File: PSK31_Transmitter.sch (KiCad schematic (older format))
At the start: 5 parts

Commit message: Add microcontroller and pll
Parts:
- added U?: CD74HCT4046AE, MODULE, symbol CD74HCT4046AE
- added U?: ATTINY24A-PU, MODULE, symbol ATTINY24A-PU
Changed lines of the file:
@@
 LIBS:valves
 LIBS:CD74HC4060E
+LIBS:CD74HCT4046AE
+LIBS:ATTINY24A-PU
+LIBS:PSK31_Transmitter-cache
 EELAYER 25 0
 EELAYER END
@@
 	1    0    0    -1
 $EndComp
+$Comp
+L CD74HCT4046AE U?
+U 1 1 5942EB48
+P 4250 4700
+F 0 "U?" H 4250 4600 50  0000 C CNN
+F 1 "CD74HCT4046AE" H 4250 4800 50  0000 C CNN
+F 2 "MODULE" H 4250 4700 50  0001 C CNN
+F 3 "DOCUMENTATION" H 4250 4700 50  0001 C CNN
+	1    4250 4700
+	1    0    0    -1
+$EndComp
+$Comp
+L ATTINY24A-PU U?
+U 1 1 5942F35B
+P 6400 3600
+F 0 "U?" H 6400 3500 50  0000 C CNN
+F 1 "ATTINY24A-PU" H 6400 3700 50  0000 C CNN
+F 2 "MODULE" H 6400 3600 50  0001 C CNN
+F 3 "DOCUMENTATION" H 6400 3600 50  0001 C CNN
+	1    6400 3600
+	1    0    0    -1
+$EndComp

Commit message: Remove counters and shift registers
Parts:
- removed U? (x3): 74HC595, symbol 74HC595
- removed U? (x2): CD74HC4060E, MODULE, symbol CD74HC4060E
- added C? (x3): C, symbol C
- added R? (x4): R, symbol R
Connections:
- net labels added: +5V, CNT0_IN, CNT0_OUT, CNT1_IN, CNT1_OUT, FREQ_OUT, GND
- wire segments 0 -> 35

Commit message: Replaced pll with dds
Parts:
- removed C? (x3): C, symbol C
- removed R? (x4): R, symbol R
- removed U?: CD74HCT4046AE, MODULE, symbol CD74HCT4046AE
- added U?: AD9834, MODULE, symbol AD9834
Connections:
- net labels removed: +5V, CNT0_IN, CNT0_OUT, CNT1_IN, CNT1_OUT, FREQ_OUT, GND
- wire segments 35 -> 0

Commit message: Replace dds with pll and prepare for new microcontroller
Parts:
- U?: value ATTINY24A-PU -> ATTINY24
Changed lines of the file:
@@
 L ATTINY24A-PU U?
 U 1 1 5942F35B
-P 1600 1250
-F 0 "U?" H 1600 1150 50  0000 C CNN
-F 1 "ATTINY24A-PU" H 1600 1350 50  0000 C CNN
-F 2 "MODULE" H 1600 1250 50  0001 C CNN
-F 3 "DOCUMENTATION" H 1600 1250 50  0001 C CNN
-	1    1600 1250
+P 1900 1550
+F 0 "U?" H 1900 1450 50  0000 C CNN
+F 1 "ATTINY24" H 1900 1650 50  0000 C CNN
+F 2 "MODULE" H 1900 1550 50  0001 C CNN
+F 3 "DOCUMENTATION" H 1900 1550 50  0001 C CNN
+	1    1900 1550
 	1    0    0    -1
 $EndComp
@@
 L AD9834 U?
 U 1 1 59445791
-P 4050 1600
-F 0 "U?" H 4050 1500 50  0000 C CNN
-F 1 "AD9834" H 4050 1700 50  0000 C CNN
-F 2 "MODULE" H 4050 1600 50  0001 C CNN
-F 3 "DOCUMENTATION" H 4050 1600 50  0001 C CNN
-	1    4050 1600
+P 3850 1600
+F 0 "U?" H 3850 1500 50  0000 C CNN
+F 1 "AD9834" H 3850 1700 50  0000 C CNN
+F 2 "MODULE" H 3850 1600 50  0001 C CNN
+F 3 "DOCUMENTATION" H 3850 1600 50  0001 C CNN
+	1    3850 1600
 	1    0    0    -1
 $EndComp

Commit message: Replace mcu and add ftdi chip
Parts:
- removed U?: ATTINY24, MODULE, symbol ATTINY24A-PU
- removed U?: AD9834, MODULE, symbol AD9834
- added C? (x3): C, symbol C
- added R?: R, symbol R
- added U?: NB3N511, MODULE, symbol NB3N511
- added U?: ADF4002, MODULE, symbol ADF4002
- added U?: ASVTX-12, MODULE, symbol ASVTX-12
- added U?: ATMEGA328P, MODULE, symbol ATMEGA328P
- added U?: FT230X, MODULE, symbol FT230X
- added Y?: Crystal, symbol Crystal
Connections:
- net labels added: +3.3V, GND
- wire segments 0 -> 14
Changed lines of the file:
@@
 LIBS:contrib
 LIBS:valves
-LIBS:ATTINY24A-PU
-LIBS:AD9834
+LIBS:NB3N511
+LIBS:ADF4002
+LIBS:ASVTX-12
+LIBS:ATMEGA328P
+LIBS:FT230X
 LIBS:PSK31_Transmitter-cache
 EELAYER 25 0
@@
 Comment4 ""
 $EndDescr
+Wire Wire Line
+	750  3050 900  3050
+Wire Wire Line
+	750  2950 750  2850
+Wire Wire Line
+	750  2950 900  2950
 $Comp
-L ATTINY24A-PU U?
-U 1 1 5942F35B
-P 1900 1550
-F 0 "U?" H 1900 1450 50  0000 C CNN
-F 1 "ATTINY24" H 1900 1650 50  0000 C CNN
-F 2 "MODULE" H 1900 1550 50  0001 C CNN
-F 3 "DOCUMENTATION" H 1900 1550 50  0001 C CNN
-	1    1900 1550
+L GND #PWR?
+U 1 1 59434A62
+P 750 3150
+F 0 "#PWR?" H 750 2900 50  0001 C CNN
+F 1 "GND" H 750 3000 50  0000 C CNN
+F 2 "" H 750 3150 50  0000 C CNN
+F 3 "" H 750 3150 50  0000 C CNN
+	1    750  3150
+	1    0    0    -1
+$EndComp
+Connection ~ 1650 1900
+Wire Wire Line
+	2400 1900 2400 2000
+Wire Wire Line
+	900  1900 900  2000
+Wire Wire Line
+	900  1900 2400 1900
+Wire Wire Line
+	1650 1950 1650 1900
+Connection ~ 900  2350
+Connection ~ 2400 2350
+Wire Wire Line
+	900  2300 900  2850
+Wire Wire Line
+	1500 2350 900  2350
+Wire Wire Line
+	2400 2350 1800 2350
+Wire Wire Line
+	2400 2300 2400 2850
+$Comp
+L GND #PWR?
+U 1 1 594348A0
+P 1650 1950
+F 0 "#PWR?" H 1650 1700 50  0001 C CNN
+F 1 "GND" H 1650 1800 50  0000 C CNN
+F 2 "" H 1650 1950 50  0000 C CNN
+F 3 "" H 1650 1950 50  0000 C CNN
+	1    1650 1950
 	1    0    0    -1
 $EndComp
 $Comp
-L AD9834 U?
-U 1 1 59445791
-P 3850 1600
-F 0 "U?" H 3850 1500 50  0000 C CNN
-F 1 "AD9834" H 3850 1700 50  0000 C CNN
-F 2 "MODULE" H 3850 1600 50  0001 C CNN
-F 3 "DOCUMENTATION" H 3850 1600 50  0001 C CNN
-	1    3850 1600
+L C C?
+U 1 1 5943486B
+P 900 2150
+F 0 "C?" H 925 2250 50  0000 L CNN
+F 1 "C" H 925 2050 50  0000 L CNN
+F 2 "" H 938 2000 50  0000 C CNN
+F 3 "" H 900 2150 50  0000 C CNN
+	1    900  2150
 	1    0    0    -1
 $EndComp
+$Comp
+L C C?
+U 1 1 594347C6
+P 2400 2150
+F 0 "C?" H 2425 2250 50  0000 L CNN
+F 1 "C" H 2425 2050 50  0000 L CNN
+F 2 "" H 2438 2000 50  0000 C CNN
+F 3 "" H 2400 2150 50  0000 C CNN
+	1    2400 2150
+	1    0    0    -1
+$EndComp
+$Comp
+L NB3N511 U?
+U 1 1 594346A4
+P 1650 3000
+F 0 "U?" H 1650 2900 50  0000 C CNN
+F 1 "NB3N511" H 1650 3100 50  0000 C CNN
+F 2 "MODULE" H 1650 3000 50  0001 C CNN
+F 3 "DOCUMENTATION" H 1650 3000 50  0001 C CNN
+	1    1650 3000
+	1    0    0    -1
+$EndComp
+$Comp
+L Crystal Y?
+U 1 1 5943440B
+P 1650 2350
+F 0 "Y?" H 1650 2500 50  0000 C CNN
+F 1 "Crystal" H 1650 2200 50  0000 C CNN
+F 2 "" H 1650 2350 50  0000 C CNN
+F 3 "" H 1650 2350 50  0000 C CNN
+	1    1650 2350
+	1    0    0    -1
+$EndComp
+$Comp
+L ADF4002 U?
+U 1 1 594372A6
+P 1700 1200
+F 0 "U?" H 1700 1100 50  0000 C CNN
+F 1 "ADF4002" H 1700 1300 50  0000 C CNN
+F 2 "MODULE" H 1700 1200 50  0001 C CNN
+F 3 "DOCUMENTATION" H 1700 1200 50  0001 C CNN
+	1    1700 1200
+	1    0    0    -1
+$EndComp
+$Comp
+L +3.3V #PWR?
+U 1 1 59437368
+P 750 2850
+F 0 "#PWR?" H 750 2700 50  0001 C CNN
+F 1 "+3.3V" H 750 2990 50  0000 C CNN
+F 2 "" H 750 2850 50  0000 C CNN
+F 3 "" H 750 2850 50  0000 C CNN
+	1    750  2850
+	1    0    0    -1
+$EndComp
+Wire Wire Line
+	750  3050 750  3150
+$Comp
+L ASVTX-12 U?
+U 1 1 59437D89
+P 3750 950
+F 0 "U?" H 3750 850 50  0000 C CNN
+F 1 "ASVTX-12" H 3750 1050 50  0000 C CNN
+F 2 "MODULE" H 3750 950 50  0001 C CNN
+F 3 "DOCUMENTATION" H 3750 950 50  0001 C CNN
+	1    3750 950
+	1    0    0    -1
+$EndComp
+$Comp
+L R R?
+U 1 1 59437F5F
+P 3600 1950
+F 0 "R?" V 3680 1950 50  0000 C CNN
+F 1 "R" V 3600 1950 50  0000 C CNN
+F 2 "" V 3530 1950 50  0000 C CNN
+F 3 "" H 3600 1950 50  0000 C CNN
+	1    3600 1950
+	0    1    1    0
+$EndComp
+$Comp
+L C C?
+U 1 1 59437FB6
+P 3400 2150
+F 0 "C?" H 3425 2250 50  0000 L CNN
+F 1 "C" H 3425 2050 50  0000 L CNN
+F 2 "" H 3438 2000 50  0000 C CNN
+F 3 "" H 3400 2150 50  0000 C CNN
+	1    3400 2150
+	1    0    0    -1
+$EndComp
+Wire Wire Line
+	3450 1950 3400 1950
+Wire Wire Line
+	3400 1950 3400 2000
+$Comp
+L ATMEGA328P U?
+U 1 1 5943B7BA
+P 7750 1450
+F 0 "U?" H 7750 1350 50  0000 C CNN
+F 1 "ATMEGA328P" H 7750 1550 50  0000 C CNN
+F 2 "MODULE" H 7750 1450 50  0001 C CNN
+F 3 "DOCUMENTATION" H 7750 1450 50  0001 C CNN
+	1    7750 1450
+	1    0    0    -1
+$EndComp
+$Comp
+L FT230X U?
+U 1 1 5943E017
+P 9600 1500
+F 0 "U?" H 9600 1400 50  0000 C CNN
+F 1 "FT230X" H 9600 1600 50  0000 C CNN
+F 2 "MODULE" H 9600 1500 50  0001 C CNN
+F 3 "DOCUMENTATION" H 9600 1500 50  0001 C CNN
+	1    9600 1500
+	1    0    0    -1
+$EndComp

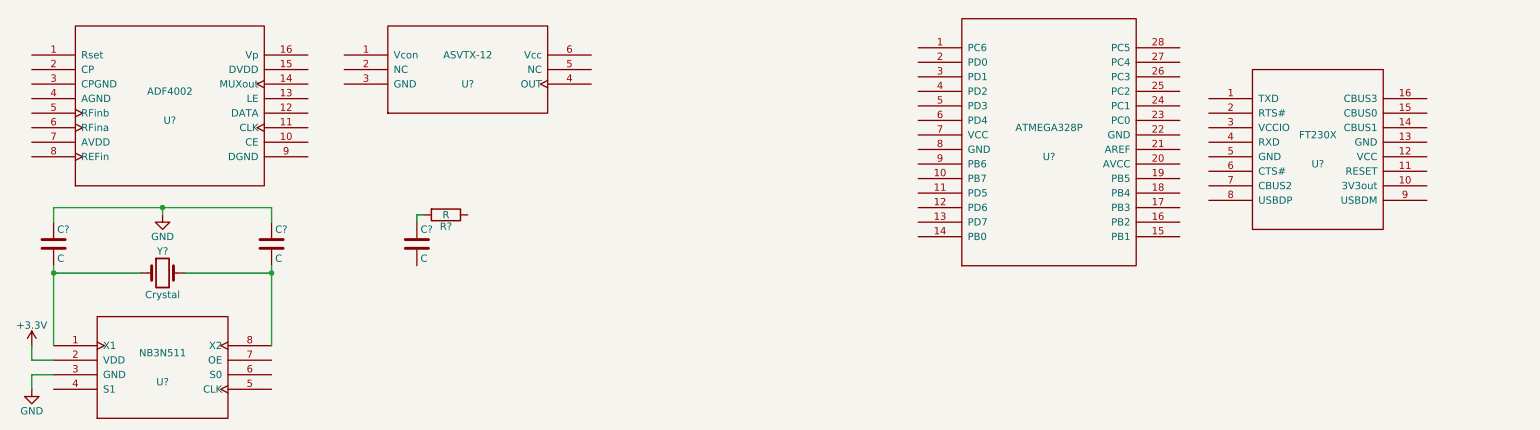
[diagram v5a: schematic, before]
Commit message: Replace pll with dds
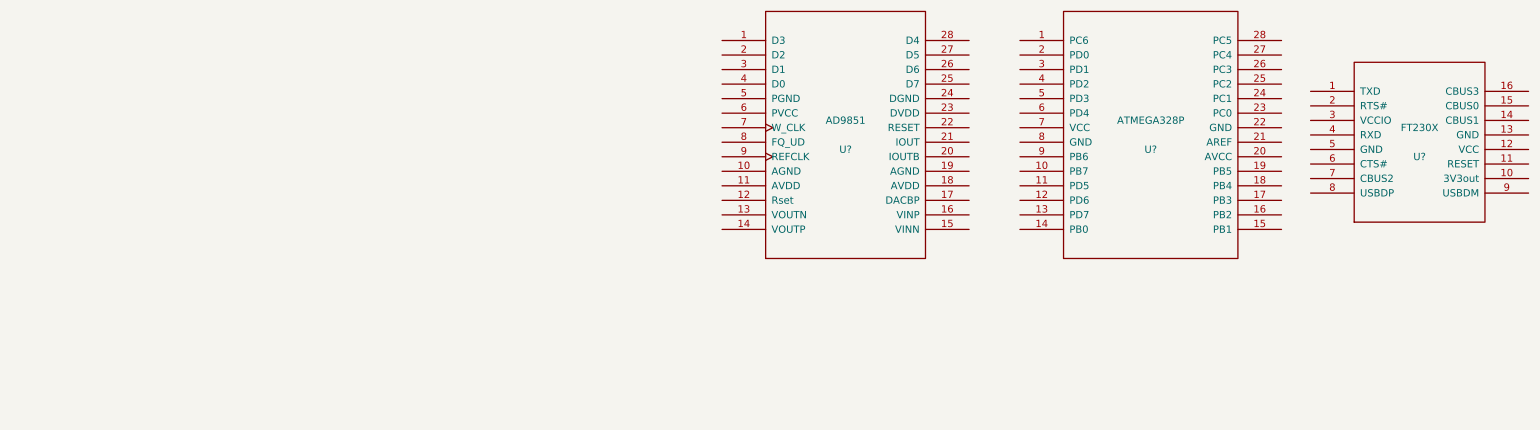
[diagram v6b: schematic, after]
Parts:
- removed C? (x3): C, symbol C
- removed R?: R, symbol R
- removed U?: NB3N511, MODULE, symbol NB3N511
- removed U?: ADF4002, MODULE, symbol ADF4002
- removed U?: ASVTX-12, MODULE, symbol ASVTX-12
- removed Y?: Crystal, symbol Crystal
- added U?: AD9851, MODULE, symbol AD9851
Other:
- moved on the sheet: U?
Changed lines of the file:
@@
 LIBS:contrib
 LIBS:valves
-LIBS:NB3N511
-LIBS:ADF4002
-LIBS:ASVTX-12
+LIBS:FT230X
 LIBS:ATMEGA328P
-LIBS:FT230X
+LIBS:AD9851
 LIBS:PSK31_Transmitter-cache
 EELAYER 25 0
@@
 Comment4 ""
 $EndDescr
-Wire Wire Line
-	750  3050 900  3050
-Wire Wire Line
-	750  2950 750  2850
-Wire Wire Line
-	750  2950 900  2950
-$Comp
-L GND #PWR?
-U 1 1 59434A62
-P 750 3150
-F 0 "#PWR?" H 750 2900 50  0001 C CNN
-F 1 "GND" H 750 3000 50  0000 C CNN
-F 2 "" H 750 3150 50  0000 C CNN
-F 3 "" H 750 3150 50  0000 C CNN
-	1    750  3150
-	1    0    0    -1
-$EndComp
-Connection ~ 1650 1900
-Wire Wire Line
-	2400 1900 2400 2000
-Wire Wire Line
-	900  1900 900  2000
-Wire Wire Line
-	900  1900 2400 1900
-Wire Wire Line
-	1650 1950 1650 1900
-Connection ~ 900  2350
-Connection ~ 2400 2350
-Wire Wire Line
-	900  2300 900  2850
-Wire Wire Line
-	1500 2350 900  2350
-Wire Wire Line
-	2400 2350 1800 2350
-Wire Wire Line
-	2400 2300 2400 2850
-$Comp
-L GND #PWR?
-U 1 1 594348A0
-P 1650 1950
-F 0 "#PWR?" H 1650 1700 50  0001 C CNN
-F 1 "GND" H 1650 1800 50  0000 C CNN
-F 2 "" H 1650 1950 50  0000 C CNN
-F 3 "" H 1650 1950 50  0000 C CNN
-	1    1650 1950
-	1    0    0    -1
-$EndComp
-$Comp
-L C C?
-U 1 1 5943486B
-P 900 2150
-F 0 "C?" H 925 2250 50  0000 L CNN
-F 1 "C" H 925 2050 50  0000 L CNN
-F 2 "" H 938 2000 50  0000 C CNN
-F 3 "" H 900 2150 50  0000 C CNN
-	1    900  2150
-	1    0    0    -1
-$EndComp
-$Comp
-L C C?
-U 1 1 594347C6
-P 2400 2150
-F 0 "C?" H 2425 2250 50  0000 L CNN
-F 1 "C" H 2425 2050 50  0000 L CNN
-F 2 "" H 2438 2000 50  0000 C CNN
-F 3 "" H 2400 2150 50  0000 C CNN
-	1    2400 2150
-	1    0    0    -1
-$EndComp
-$Comp
-L NB3N511 U?
-U 1 1 594346A4
-P 1650 3000
-F 0 "U?" H 1650 2900 50  0000 C CNN
-F 1 "NB3N511" H 1650 3100 50  0000 C CNN
-F 2 "MODULE" H 1650 3000 50  0001 C CNN
-F 3 "DOCUMENTATION" H 1650 3000 50  0001 C CNN
-	1    1650 3000
-	1    0    0    -1
-$EndComp
-$Comp
-L Crystal Y?
-U 1 1 5943440B
-P 1650 2350
-F 0 "Y?" H 1650 2500 50  0000 C CNN
-F 1 "Crystal" H 1650 2200 50  0000 C CNN
-F 2 "" H 1650 2350 50  0000 C CNN
-F 3 "" H 1650 2350 50  0000 C CNN
-	1    1650 2350
-	1    0    0    -1
-$EndComp
-$Comp
-L ADF4002 U?
-U 1 1 594372A6
-P 1700 1200
-F 0 "U?" H 1700 1100 50  0000 C CNN
-F 1 "ADF4002" H 1700 1300 50  0000 C CNN
-F 2 "MODULE" H 1700 1200 50  0001 C CNN
-F 3 "DOCUMENTATION" H 1700 1200 50  0001 C CNN
-	1    1700 1200
-	1    0    0    -1
-$EndComp
-$Comp
-L +3.3V #PWR?
-U 1 1 59437368
-P 750 2850
-F 0 "#PWR?" H 750 2700 50  0001 C CNN
-F 1 "+3.3V" H 750 2990 50  0000 C CNN
-F 2 "" H 750 2850 50  0000 C CNN
-F 3 "" H 750 2850 50  0000 C CNN
-	1    750  2850
-	1    0    0    -1
-$EndComp
-Wire Wire Line
-	750  3050 750  3150
-$Comp
-L ASVTX-12 U?
-U 1 1 59437D89
-P 3750 950
-F 0 "U?" H 3750 850 50  0000 C CNN
-F 1 "ASVTX-12" H 3750 1050 50  0000 C CNN
-F 2 "MODULE" H 3750 950 50  0001 C CNN
-F 3 "DOCUMENTATION" H 3750 950 50  0001 C CNN
-	1    3750 950
-	1    0    0    -1
-$EndComp
-$Comp
-L R R?
-U 1 1 59437F5F
-P 3600 1950
-F 0 "R?" V 3680 1950 50  0000 C CNN
-F 1 "R" V 3600 1950 50  0000 C CNN
-F 2 "" V 3530 1950 50  0000 C CNN
-F 3 "" H 3600 1950 50  0000 C CNN
-	1    3600 1950
-	0    1    1    0
-$EndComp
-$Comp
-L C C?
-U 1 1 59437FB6
-P 3400 2150
-F 0 "C?" H 3425 2250 50  0000 L CNN
-F 1 "C" H 3425 2050 50  0000 L CNN
-F 2 "" H 3438 2000 50  0000 C CNN
-F 3 "" H 3400 2150 50  0000 C CNN
-	1    3400 2150
-	1    0    0    -1
-$EndComp
-Wire Wire Line
-	3450 1950 3400 1950
-Wire Wire Line
-	3400 1950 3400 2000
 $Comp
 L ATMEGA328P U?
 U 1 1 5943B7BA
-P 7750 1450
-F 0 "U?" H 7750 1350 50  0000 C CNN
-F 1 "ATMEGA328P" H 7750 1550 50  0000 C CNN
-F 2 "MODULE" H 7750 1450 50  0001 C CNN
-F 3 "DOCUMENTATION" H 7750 1450 50  0001 C CNN
-	1    7750 1450
+P 8450 1400
+F 0 "U?" H 8450 1300 50  0000 C CNN
+F 1 "ATMEGA328P" H 8450 1500 50  0000 C CNN
+F 2 "MODULE" H 8450 1400 50  0001 C CNN
+F 3 "DOCUMENTATION" H 8450 1400 50  0001 C CNN
+	1    8450 1400
 	1    0    0    -1
 $EndComp
@@
 L FT230X U?
 U 1 1 5943E017
-P 9600 1500
-F 0 "U?" H 9600 1400 50  0000 C CNN
-F 1 "FT230X" H 9600 1600 50  0000 C CNN
-F 2 "MODULE" H 9600 1500 50  0001 C CNN
-F 3 "DOCUMENTATION" H 9600 1500 50  0001 C CNN
-	1    9600 1500
+P 10300 1450
+F 0 "U?" H 10300 1350 50  0000 C CNN
+F 1 "FT230X" H 10300 1550 50  0000 C CNN
+F 2 "MODULE" H 10300 1450 50  0001 C CNN
+F 3 "DOCUMENTATION" H 10300 1450 50  0001 C CNN
+	1    10300 1450
 	1    0    0    -1
 $EndComp
+$Comp
+L AD9851 U?
+U 1 1 5948AB39
+P 6350 1400
+F 0 "U?" H 6350 1300 50  0000 C CNN
+F 1 "AD9851" H 6350 1500 50  0000 C CNN
+F 2 "MODULE" H 6350 1400 50  0001 C CNN
+F 3 "DOCUMENTATION" H 6350 1400 50  0001 C CNN
+	1    6350 1400
+	1    0    0    -1
+$EndComp

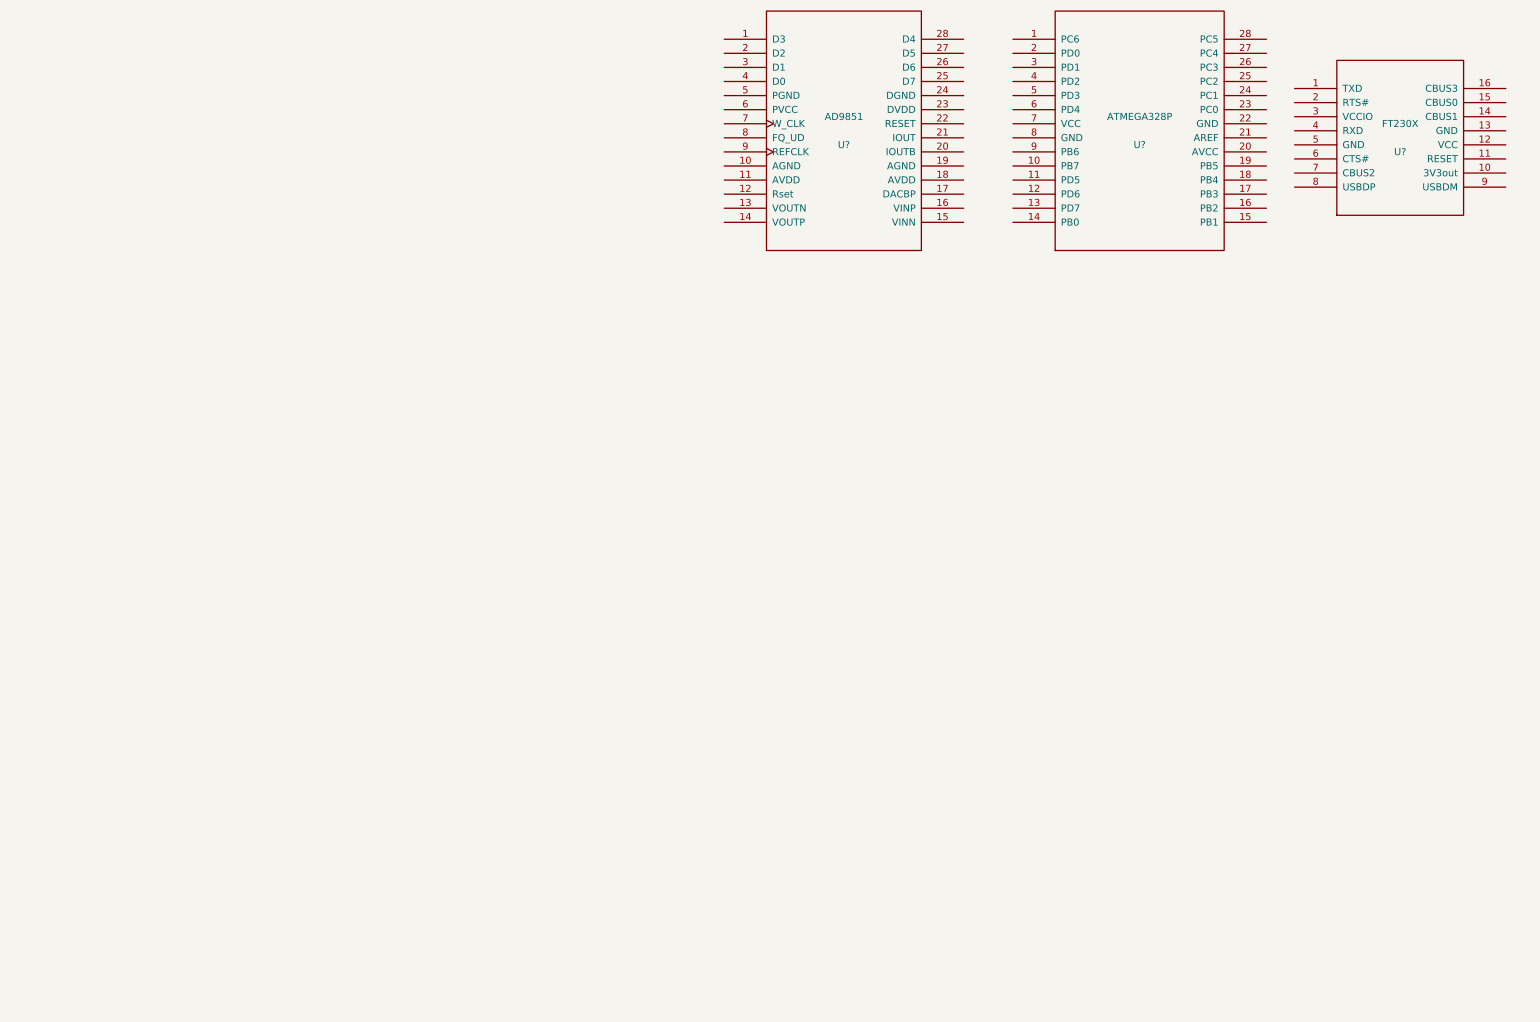
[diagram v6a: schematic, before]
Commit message: Add filters and amplifer
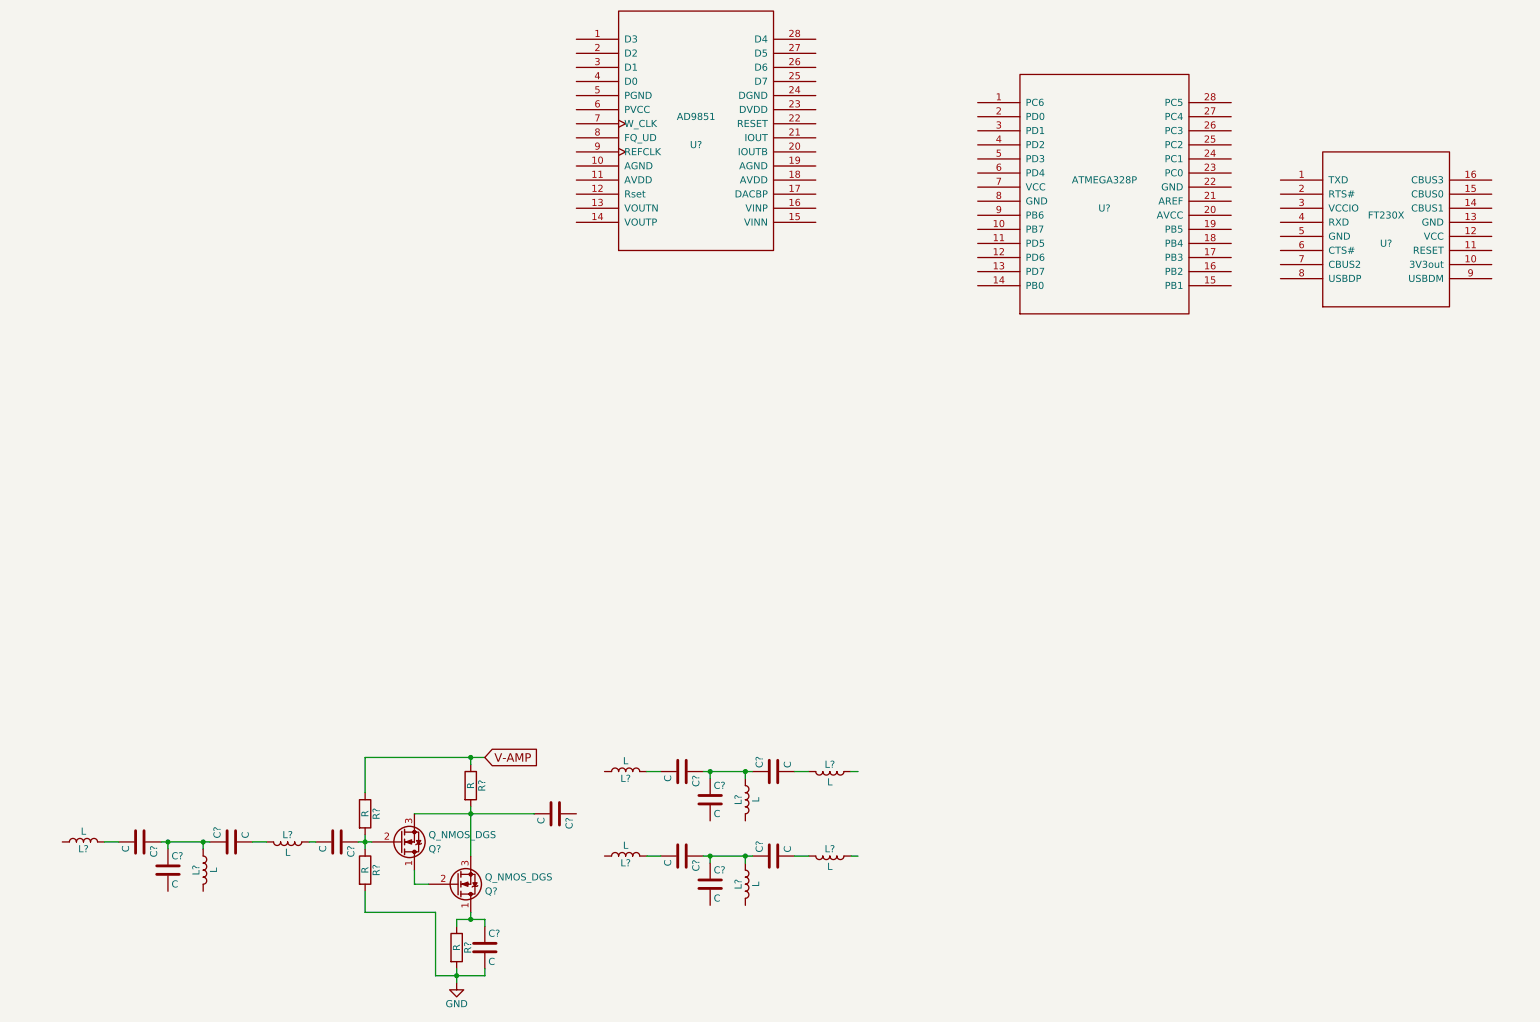
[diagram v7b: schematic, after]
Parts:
- added C? (x12): C, symbol C
- added L? (x9): L, symbol L
- added Q? (x2): Q_NMOS_DGS, symbol Q_NMOS_DGS
- added R? (x4): R, symbol R
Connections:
- net labels added: GND, V-AMP
- wire segments 0 -> 37
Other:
- moved on the sheet: U?
